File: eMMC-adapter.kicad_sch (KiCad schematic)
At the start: 61 parts, among them J2 Conn_Coaxial, U1 ESP32-PICO-D4

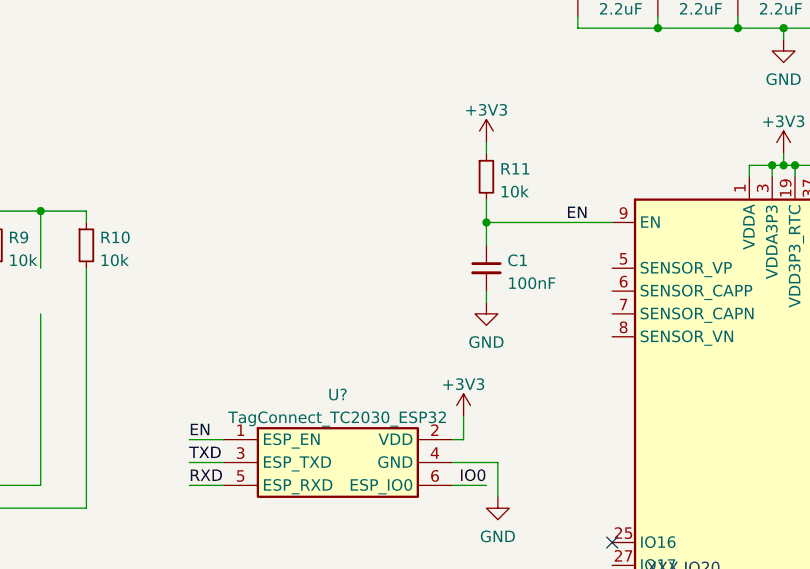
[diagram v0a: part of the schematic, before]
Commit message: Add project icon to PCB
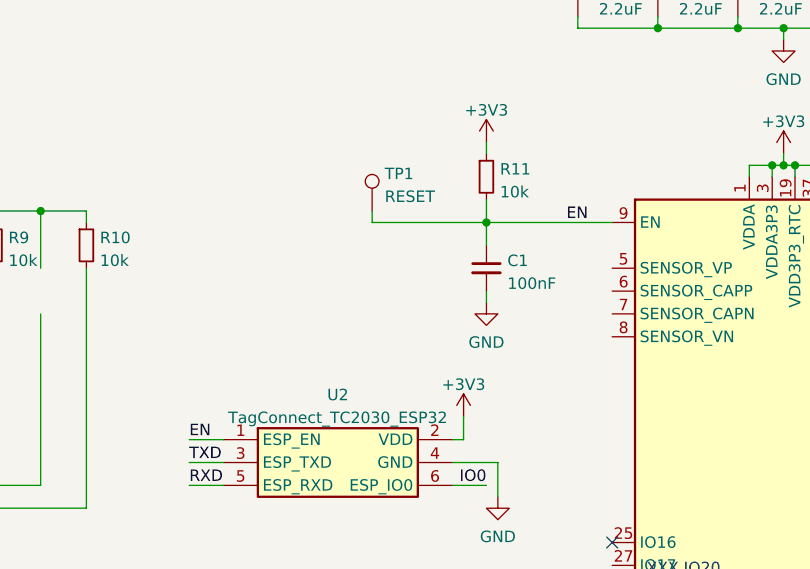
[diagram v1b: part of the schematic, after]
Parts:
- added TP1: RESET, TestPoint:TestPoint_Pad_D1.0mm, symbol Connector:TestPoint
- gave numbers to parts that had none: 1
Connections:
- net EN: now also TP1.1
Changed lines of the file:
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@@
+    (stroke (width 0) (type default) (color 0 0 0 0))
+  )
+  (wire (pts (xy 156.21 71.12) (xy 168.91 71.12))
     (stroke (width 0) (type default) (color 0 0 0 0))
   )
@@
   )
   (wire (pts (xy 246.38 71.12) (xy 246.38 72.39))
+    (stroke (width 0) (type default) (color 0 0 0 0))
+  )
+  (wire (pts (xy 156.21 71.12) (xy 156.21 69.85))
     (stroke (width 0) (type default) (color 0 0 0 0))
   )
@@
   (symbol (lib_id "Connector_TagConnect:TagConnect_TC2030_ESP32") (at 152.4 97.79 0) (unit 1)
     (in_bom yes) (on_board yes) (fields_autoplaced)
-    (property "Reference" "U?" (id 0) (at 152.4 90.2802 0))
+    (property "Reference" "U2" (id 0) (at 152.4 90.2802 0))
     (property "Value" "TagConnect_TC2030_ESP32" (id 1) (at 152.4 92.8171 0))
     (property "Footprint" "Connector:Tag-Connect_TC2030-IDC-NL_2x03_P1.27mm_Vertical" (id 2) (at 152.4 97.79 0)
@@
     (pin "2")
   )
+  (symbol (lib_id "Connector:TestPoint") (at 156.21 69.85 0) (unit 1)
+    (in_bom yes) (on_board yes) (fields_autoplaced)
+    (property "Reference" "TP1" (id 0) (at 157.607 65.7133 0)
+      (effects (font (size 1.27 1.27)) (justify left))
+    )
+    (property "Value" "RESET" (id 1) (at 157.607 68.2502 0)
+      (effects (font (size 1.27 1.27)) (justify left))
+    )
+    (property "Footprint" "TestPoint:TestPoint_Pad_D1.0mm" (id 2) (at 161.29 69.85 0)
+      (effects (font (size 1.27 1.27)) hide)
+    )
+    (property "Datasheet" "~" (id 3) (at 161.29 69.85 0)
+      (effects (font (size 1.27 1.27)) hide)
+    )
+    (pin "1")
+  )
   (symbol (lib_id "Device:R_Small") (at 82.55 85.09 270) (unit 1)
